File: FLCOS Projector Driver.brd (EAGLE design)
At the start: 73.9 x 62.1 mm, 68 parts, among them IC1 LM1117MPX-3.3, IC2 MIC5323-1.8YD5-TR, IC3 MIC5504-2.5YM5-TR, IC4 TVP5150-NTSC_DECODER, IC5 CH340G, IC6 ESP32-WROOM-32U, IC7 LM3414, IC8 LM3414, IC9 LM3414, J1 MEM2075-00-140-01-A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

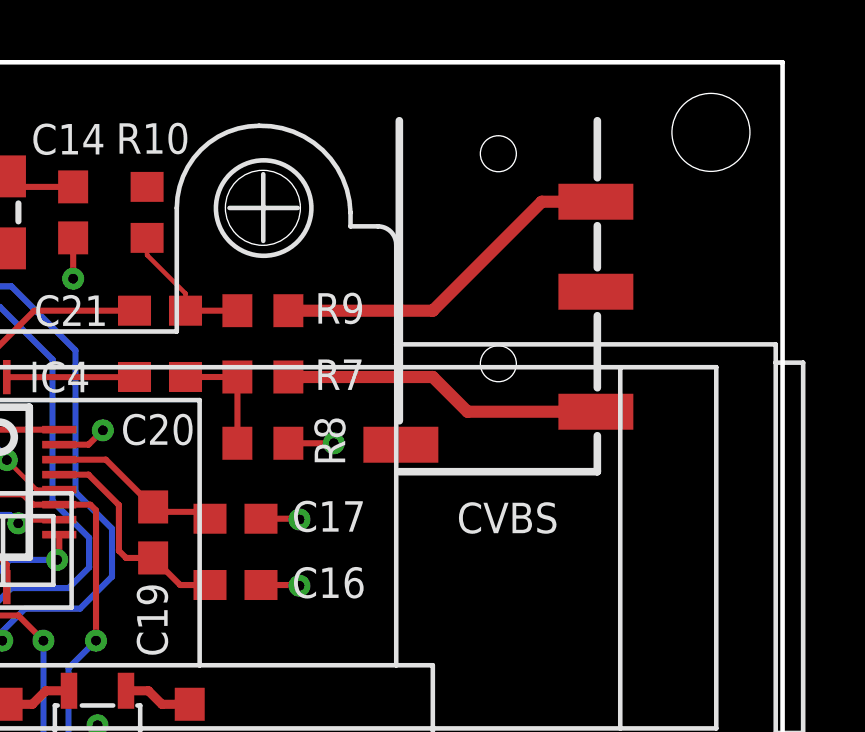
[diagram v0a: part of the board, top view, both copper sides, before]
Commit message: Added Mouser cart XLS. BOM tweaks due to low stocks
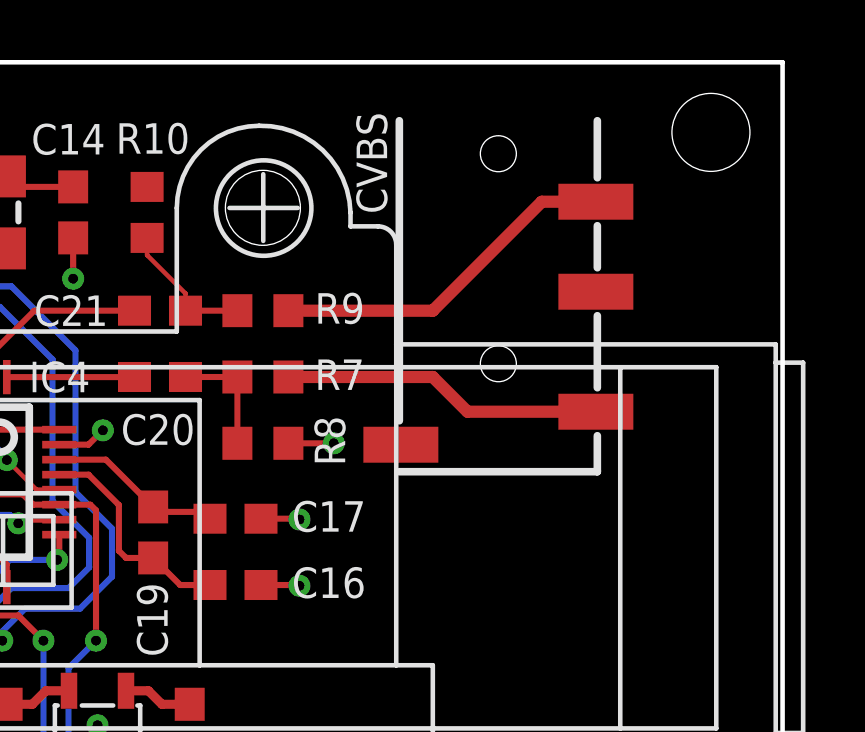
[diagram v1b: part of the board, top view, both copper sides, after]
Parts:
- IC1: value LM1117MPX-3.3 -> TLV1117LV33DCYT
- IC6: value ESP32-WROOM-32U -> ESP32-WROOM-32UE-N4
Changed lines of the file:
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@@
 <attribute name="VALUE" x="29.8958" y="38.5826" size="1.27" layer="27"/>
 </element>
-<element name="IC6" library="ESP32-WROOM-32U" package="ESP32WROOM32D" value="ESP32-WROOM-32U" x="18.034" y="46.9392" smashed="yes" rot="R180">
+<element name="IC6" library="ESP32-WROOM-32U" package="ESP32WROOM32D" value="ESP32-WROOM-32UE-N4" x="18.034" y="46.9392" smashed="yes" rot="R180">
 <attribute name="DESCRIPTION" value="WiFi Modules (802.11) SMD Module, ESP32-D0WD, 32Mbits SPI flash, UART mode, U.FL antenna connector" x="36.9316" y="132.7404" size="1.778" layer="27" rot="R180" display="off"/>
 <attribute name="HEIGHT" value="3.1mm" x="36.9316" y="132.7404" size="1.778" layer="27" rot="R180" display="off"/>
@@
 <attribute name="VALUE" x="35.7632" y="22.387559375" size="1.27" layer="27" rot="R90"/>
 </element>
-<element name="IC1" library="SparkFun" package="SOT223" value="LM1117MPX-3.3" x="29.4132" y="30.7476" smashed="yes" rot="R270">
+<element name="IC1" library="SparkFun" package="SOT223" value="TLV1117LV33DCYT" x="29.4132" y="30.7476" smashed="yes" rot="R270">
 <attribute name="NAME" x="34.1503" y="31.8017" size="1.016" layer="25" rot="R270"/>
 <attribute name="VALUE" x="29.2227" y="31.8271" size="0.4064" layer="27" rot="R270"/>
@@
 </element>
 <element name="CVBS" library="SparkFun-Connectors" package="AUDIO_JACK_3.5MM_TRRS_SMD_RA" value="AUDIO_JACK_TRRSSMD_RA" x="68.8086" y="64.4652" smashed="yes" rot="R270">
-<attribute name="NAME" x="70.8152" y="51.2318" size="1.016" layer="25" ratio="20" rot="R180"/>
+<attribute name="NAME" x="65.1002" y="60.8584" size="1.016" layer="25" ratio="20" rot="R90"/>
 <attribute name="PROD_ID" value="CONN-10676" x="68.8086" y="64.4652" size="1.016" layer="27" rot="R270" display="off"/>
 <attribute name="SF_ID" value="PRT-12639" x="68.8086" y="64.4652" size="1.016" layer="27" rot="R270" display="off"/>

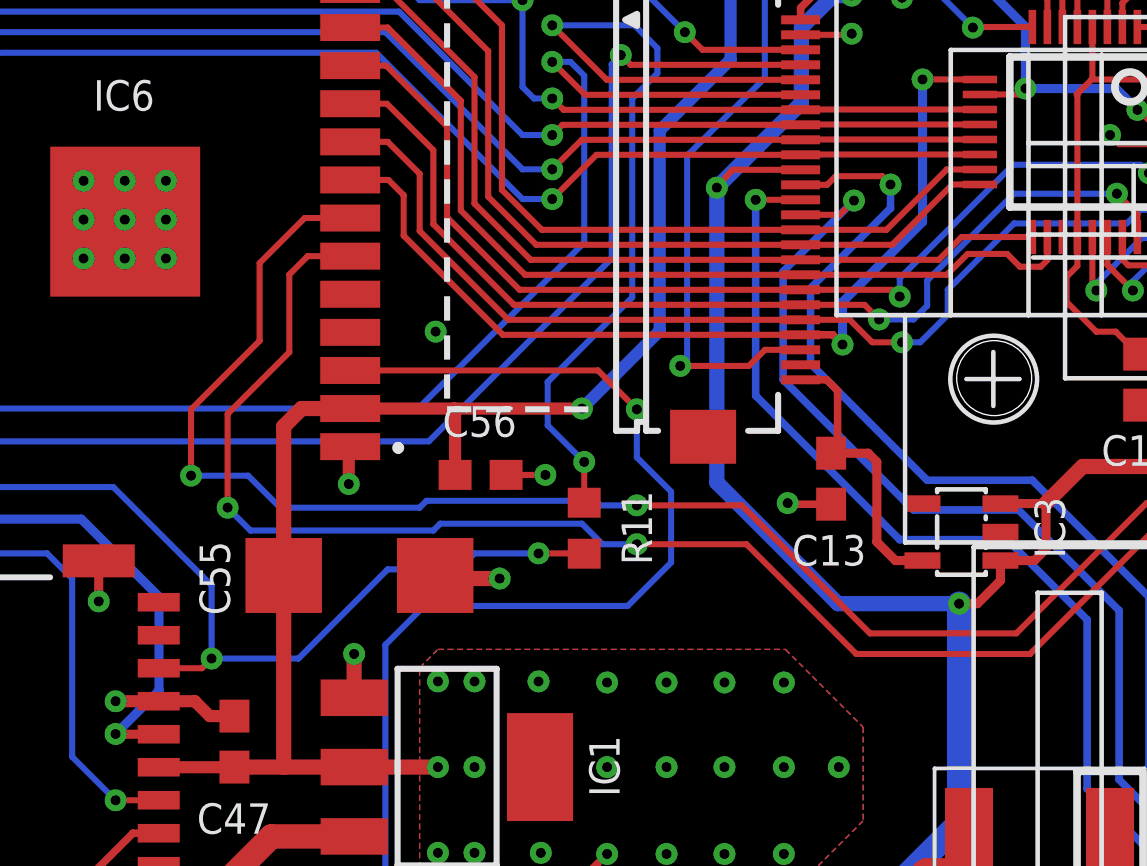
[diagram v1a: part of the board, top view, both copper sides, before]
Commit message: Changed R11 to a pull-up for FLCOS_SOUT
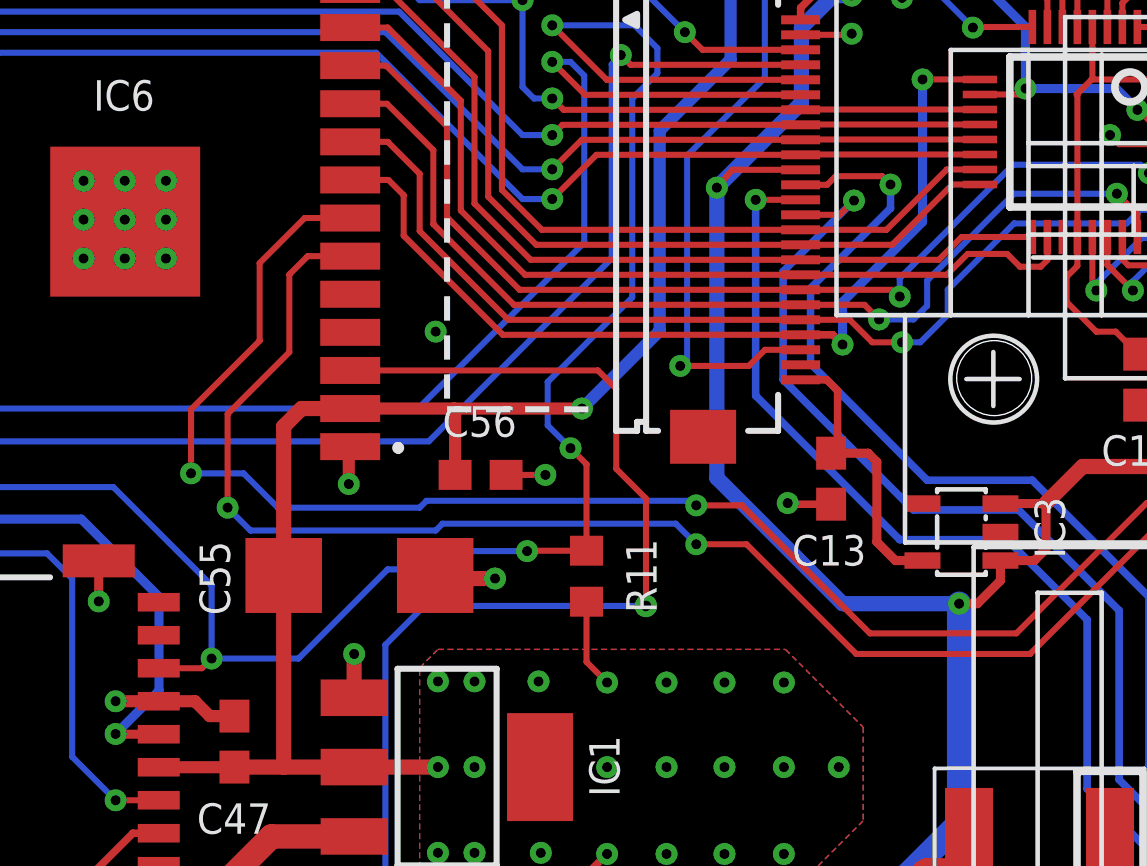
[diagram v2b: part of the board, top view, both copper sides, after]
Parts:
- R11: value 37R4 -> 2K2
- moved R11 1.60 mm to (34.1, 37.1), turned to 270 degrees
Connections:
- removed net FLCOS_SOUT: FPC.5, R11.2
- net +3V3: now also R11.2
- net SPI_MISO: now also FPC.5
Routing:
- net SPI_MISO: track 41.6 -> 73.4 mm, vias 3 -> 5
- net FLCOS_SOUT: track 30.0 -> 0.00 mm, vias 2 -> 0
- net +3V3: track 107.7 -> 110.7 mm

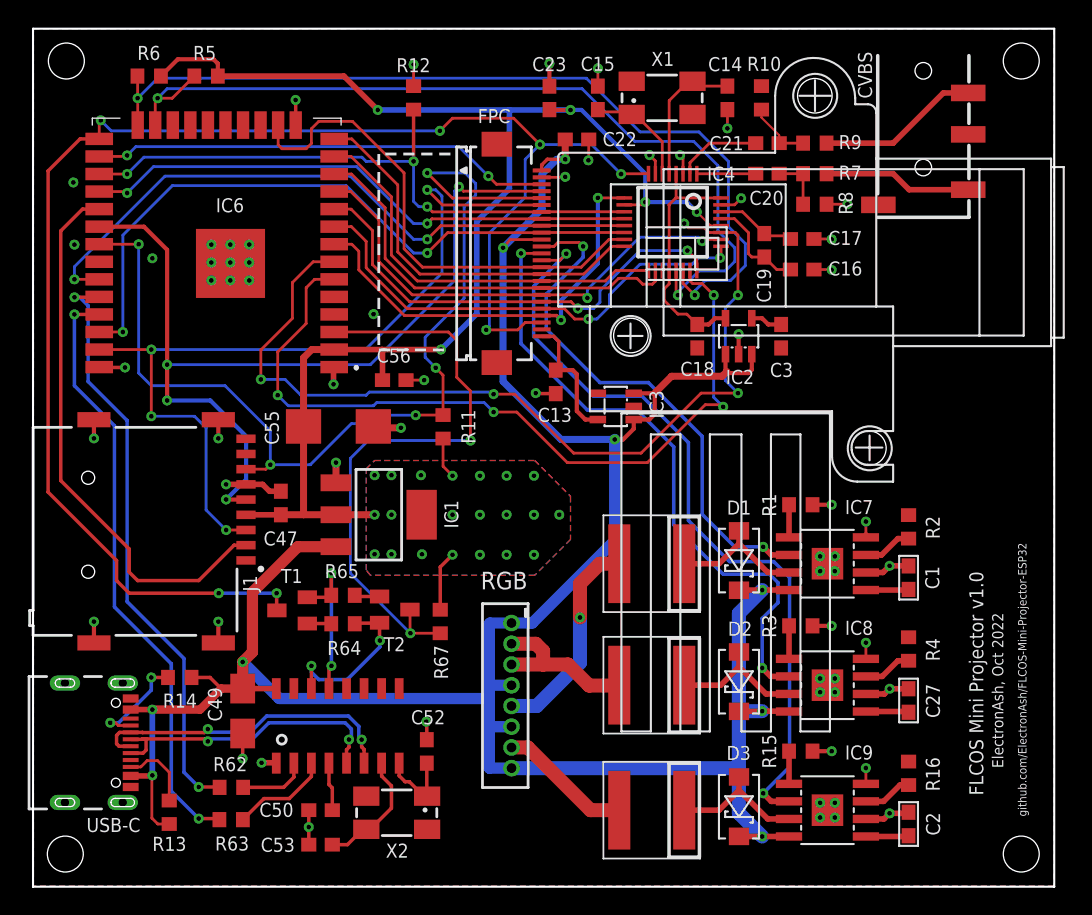
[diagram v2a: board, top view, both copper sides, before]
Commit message: Added inverter transistors for RGB LED PWM signals
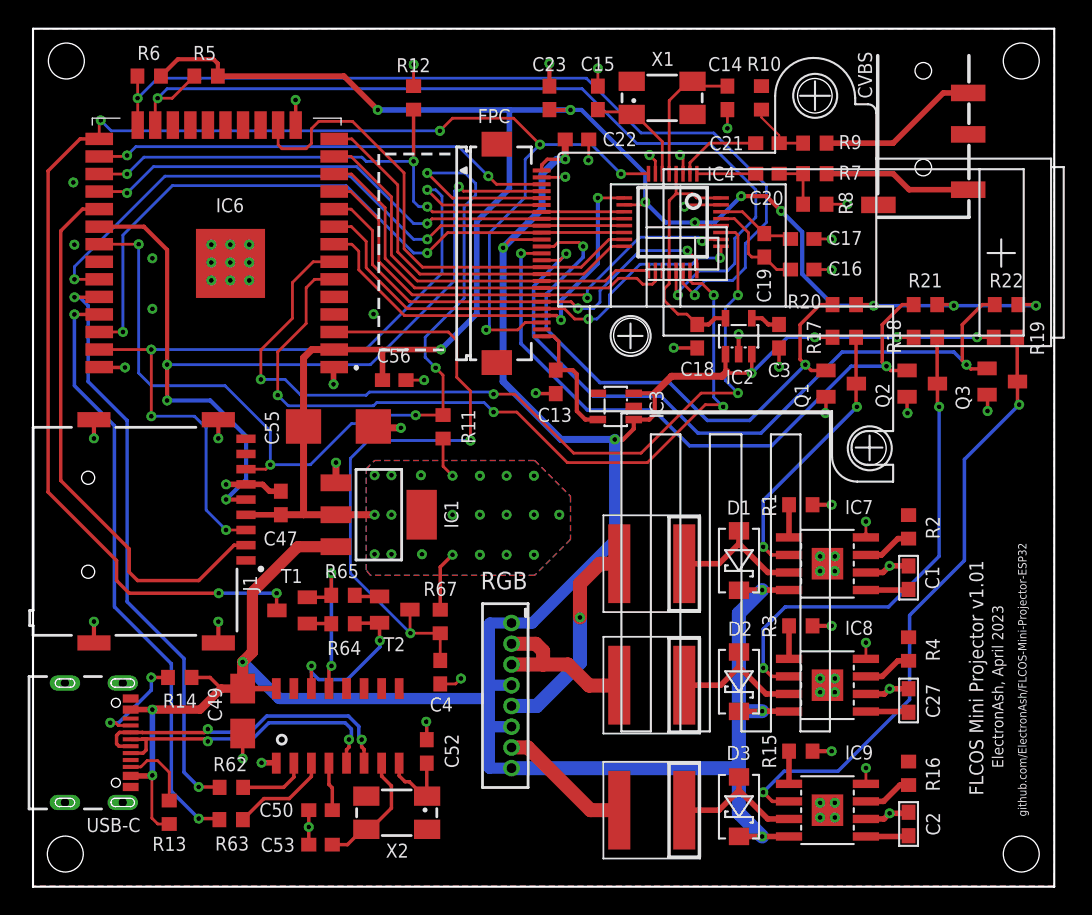
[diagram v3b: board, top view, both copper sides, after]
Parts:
- added C4: 100nF, rcl:C0603
- added Q1, Q2, Q3: BC849SMD, transistor-npn:SOT23-BEC
- added R17, R18, R19, R20, R21, R22: 2K2, rcl:R0603
- R67: value 2K2 -> 12K
- T1, T2: device transistor:SOT23 -> transistor-npn:SOT23-BEC
- moved C3 0.15 mm to (58.4, 43.7)
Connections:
- new net N$1: IC7.6, Q1.C, R17.1
- new net N$11: IC8.6, Q2.C, R18.1
- new net N$12: IC9.6, Q3.C, R19.1
- net +3V3: now also R20.2, R21.2, R22.2
- net +5V: now also R17.2, R18.2, R19.2
- net BLU_PWM: now also Q3.B, R22.1; no longer IC9.6
- net ESP_EN_N: now also C4.2, T2.C; no longer T2.3
- net GND: now also C4.1, Q1.E, Q2.E, Q3.E
- net GRN_PWM: now also Q2.B, R21.1; no longer IC8.6
- net N$71: now also T1.B; no longer T1.1
- net N$77: now also T2.B; no longer T2.1
- net N$78: now also T2.E; no longer T2.2
- net N$79: now also T1.E; no longer T1.2
- net RED_PWM: now also Q1.B, R20.1; no longer IC7.6
- net TVP_FL_RST_N: now also T1.C; no longer T1.3
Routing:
- net N$12: track 0.00 -> 45.1 mm, vias 0 -> 2
- net N$11: track 0.00 -> 35.7 mm, vias 0 -> 2
- net +3V3: track 110.7 -> 145.1 mm, vias 26 -> 31
- net +5V: track 192.7 -> 214.1 mm, vias 9 -> 13
- net N$1: track 0.00 -> 20.1 mm, vias 0 -> 2
- net GND: track 64.8 -> 74.2 mm, vias 63 -> 70
- net RED_PWM: track 37.9 -> 41.1 mm
- net BLU_PWM: track 56.5 -> 53.6 mm
- net TVP_INT: track 66.7 -> 63.8 mm, vias 5 -> 4
- net ESP_EN_N: track 44.4 -> 46.3 mm
- net TVP_SDA: track 64.3 -> 66.2 mm
- net TVP_SCL: track 63.0 -> 64.9 mm
- net GRN_PWM: track 45.9 -> 47.5 mm
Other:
- board text added: "ElectronAsh, April 2023"
- board text added: "FLCOS Mini Projector v1.01"
- board text removed: "ElectronAsh, Oct 2022"
- board text removed: "FLCOS Mini Projector v1.0"

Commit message: PCB changes to fix auto-reset during Flash programming
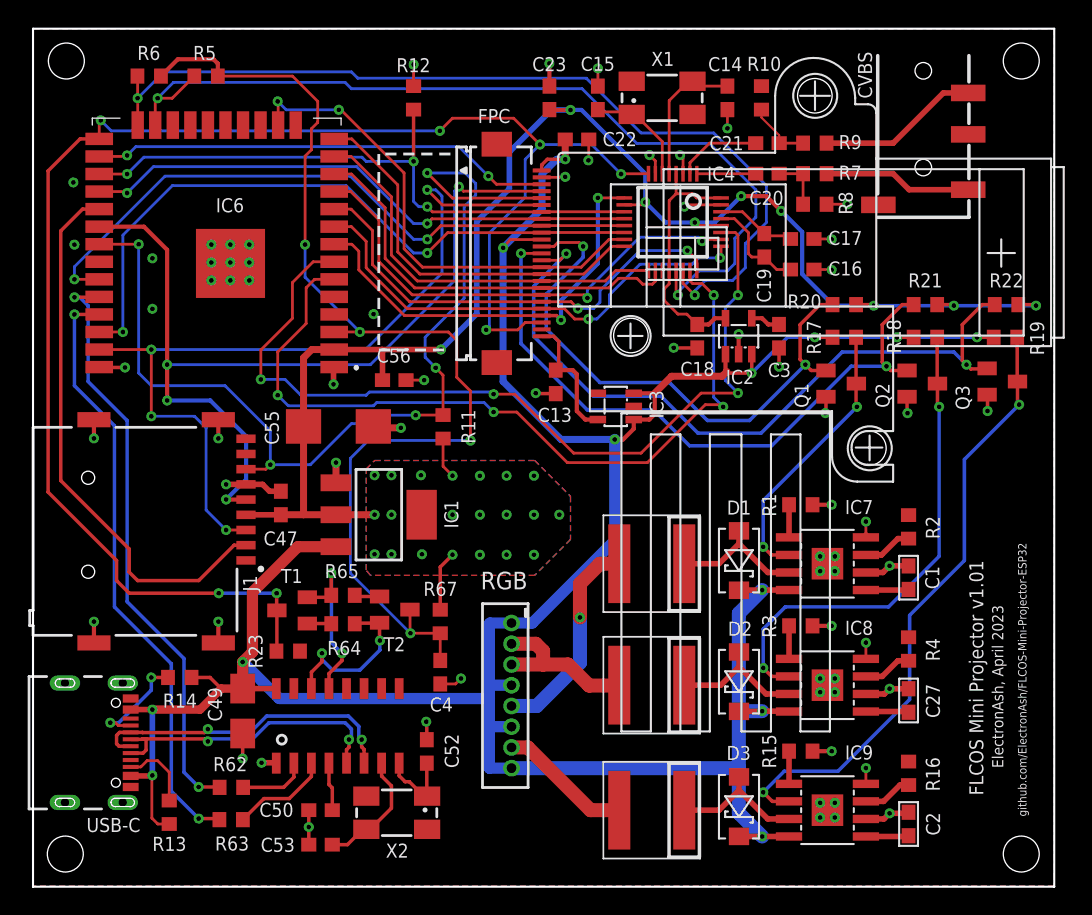
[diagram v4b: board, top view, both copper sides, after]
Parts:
- added R23: 2K2, rcl:R0603
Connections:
- net +3V3: no longer R5.2, R6.2
- net ESP_EN_N: now also R5.2, R6.2
- net GND: now also R23.1
- net TVP_FL_RST_N: now also R23.2
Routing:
- net ESP_EN_N: track 46.3 -> 78.7 mm, vias 2 -> 4
- net +3V3: track 145.1 -> 115.5 mm, vias 31 -> 30
- net TVP_FL_RST_N: track 112.2 -> 115.2 mm
- net GND: track 74.2 -> 72.4 mm, vias 70 -> 69
- net FLCOS_D3: track 36.5 -> 35.8 mm, vias 0 -> 2
- net N$79: track 11.8 -> 12.5 mm
